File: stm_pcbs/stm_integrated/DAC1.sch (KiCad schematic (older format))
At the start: 21 parts, among them P2 BNC, U4 AD8676, U5 AD5791, U6 AD8675

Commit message: working on Kicad of 3rd Dec
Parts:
- C17, C19, C21, C23, C24, C27, C28, C31, C32: symbol C -> device:C
- C18, C20, C22, C25, C26, C29, C30: symbol CP2 -> device:CP1
- P2: symbol BNC -> device:BNC
- R2: symbol R -> device:R
- U4: symbol AD8676 -> ad5791:AD8676
- U5: symbol AD5791 -> ad5791:AD5791
- U6: symbol AD8675 -> ad5791:AD8675
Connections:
- wire segments 113 -> 128

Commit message: fixing more borkage
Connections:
- net labels added: +5V
- net labels removed: 3.3V
- wire segments 128 -> 123
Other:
- moved on the sheet: C21, C22, R2
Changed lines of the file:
@@
 Text GLabel 5350 4950 2    60   Input ~ 0
 -14V
-Text GLabel 4250 2400 0    60   Input ~ 0
-3.3V
 $Comp
 L power:AGND #PWR014
@@
 L device:C C21
 U 1 1 5A25DC09
-P 6000 4700
+P 6000 4650
 AR Path="/5A25DC09" Ref="C21"  Part="1"
 AR Path="/5A25907D/5A25DC09" Ref="C21"  Part="1"
-F 0 "C21" H 6000 4800 40  0000 L CNN
-F 1 "0.1uF" H 6006 4615 40  0000 L CNN
-F 2 "Capacitors_SMD:C_0805_HandSoldering" H 6038 4550 30  0001 C CNN
-F 3 "" H 6000 4700 60  0000 C CNN
-	1    6000 4700
+F 0 "C21" H 6000 4750 40  0000 L CNN
+F 1 "0.1uF" H 6006 4565 40  0000 L CNN
+F 2 "Capacitors_SMD:C_0805_HandSoldering" H 6038 4500 30  0001 C CNN
+F 3 "" H 6000 4650 60  0000 C CNN
+	1    6000 4650
 	0    1    1    0
 $EndComp
@@
 L device:CP1 C22
 U 1 1 5A25DC67
-P 6000 4950
+P 6000 5000
 AR Path="/5A25DC67" Ref="C22"  Part="1"
 AR Path="/5A25907D/5A25DC67" Ref="C22"  Part="1"
-F 0 "C22" H 6000 5050 40  0000 L CNN
-F 1 "10uF" H 6006 4865 40  0000 L CNN
-F 2 "stm:SMD-1210_Pol" H 6038 4800 30  0001 C CNN
-F 3 "" H 6000 4950 60  0000 C CNN
-	1    6000 4950
+F 0 "C22" H 6000 5100 40  0000 L CNN
+F 1 "10uF" H 6006 4915 40  0000 L CNN
+F 2 "stm:SMD-1210_Pol" H 6038 4850 30  0001 C CNN
+F 3 "" H 6000 5000 60  0000 C CNN
+	1    6000 5000
 	0    1    1    0
 $EndComp
@@
 	7850 3750 7850 3900
 Wire Wire Line
-	5600 2050 5600 2300
-Wire Wire Line
 	5300 4800 5300 4950
 Wire Wire Line
@@
 Connection ~ 4650 2500
 Wire Wire Line
-	4400 2400 4250 2400
-Wire Wire Line
 	4850 5000 4850 4800
 Wire Wire Line
@@
 Wire Wire Line
 	5250 2450 5250 2700
-Wire Wire Line
-	5600 2300 5700 2300
-Connection ~ 5600 2300
 Wire Wire Line
 	5650 2550 5650 2400
@@
 Wire Wire Line
 	5300 4800 5800 4800
-Wire Wire Line
-	5800 4700 5800 4800
-Wire Wire Line
-	6200 4700 6200 4800
 Connection ~ 5800 4800
 Wire Wire Line
@@
 L device:R R2
 U 1 1 5A25DD1F
-P 7150 4650
+P 7150 4550
 AR Path="/5A25DD1F" Ref="R2"  Part="1"
 AR Path="/5A25907D/5A25DD1F" Ref="R2"  Part="1"
-F 0 "R2" V 7230 4650 40  0000 C CNN
-F 1 "0" V 7157 4651 40  0000 C CNN
-F 2 "stm:0Ohm" V 7080 4650 30  0001 C CNN
-F 3 "" H 7150 4650 30  0000 C CNN
-	1    7150 4650
+F 0 "R2" V 7230 4550 40  0000 C CNN
+F 1 "0" V 7157 4551 40  0000 C CNN
+F 2 "stm:0Ohm" V 7080 4550 30  0001 C CNN
+F 3 "" H 7150 4550 30  0000 C CNN
+	1    7150 4550
 	0    1    1    0
 $EndComp
@@
 $EndComp
 Wire Wire Line
-	7400 4750 7400 4650
-Wire Wire Line
-	6900 4650 6900 4750
-Wire Wire Line
-	7600 3750 7600 3800
-Wire Wire Line
-	7600 4150 7600 4100
-Wire Wire Line
-	7400 4650 7300 4650
-Wire Wire Line
-	7000 4650 6900 4650
-Wire Wire Line
-	6150 4700 6200 4700
-Wire Wire Line
-	5850 4700 5800 4700
-Wire Wire Line
-	7600 3000 7600 3050
-Wire Wire Line
-	7600 3400 7600 3350
-Wire Wire Line
 	3850 2150 3850 2200
 Wire Wire Line
 	3850 1850 3850 1800
-Wire Wire Line
-	6000 2300 6050 2300
 Wire Wire Line
 	3200 3300 3850 3300
@@
 	4650 2500 4800 2500
 Wire Wire Line
+	5600 2400 5600 2450
+Wire Wire Line
+	6050 2400 6050 2550
+Wire Wire Line
+	4450 2500 4650 2500
+Wire Wire Line
+	3950 1800 4100 1800
+Wire Wire Line
+	7600 5350 7700 5350
+Wire Wire Line
+	7250 5500 7350 5500
+Wire Wire Line
+	7250 5900 7350 5900
+Wire Wire Line
+	8600 5350 8750 5350
+Wire Wire Line
+	7700 5350 7800 5350
+Wire Wire Line
+	6850 3200 6950 3200
+Wire Wire Line
+	6850 3900 6900 3900
+Wire Wire Line
+	8750 6300 8750 6350
+Wire Wire Line
+	8750 5750 8750 5800
+Wire Wire Line
+	3850 2200 4100 2200
+Wire Wire Line
+	7250 6050 7700 6050
+Wire Wire Line
+	7700 6050 7800 6050
+Wire Wire Line
+	6850 3000 7400 3000
+Wire Wire Line
+	6850 3750 7400 3750
+Wire Wire Line
+	7750 5900 8750 5900
+Wire Wire Line
+	7300 3400 7400 3400
+Wire Wire Line
+	7400 4550 7400 4750
+Wire Wire Line
+	6900 4550 6900 4750
+Wire Wire Line
+	6200 4800 6200 5000
+Wire Wire Line
+	5800 4800 5800 5000
+Wire Wire Line
+	6200 4650 6200 4800
+Wire Wire Line
+	5800 4650 5800 4800
+Connection ~ 7400 3000
+Wire Wire Line
+	7400 3000 7600 3000
+Connection ~ 7400 3400
+Wire Wire Line
+	7400 3400 7600 3400
+Connection ~ 7400 3750
+Wire Wire Line
+	7400 3750 7600 3750
+Connection ~ 7400 4150
+Wire Wire Line
+	5600 2050 5600 2300
+Wire Wire Line
+	5650 2300 5600 2300
+Connection ~ 5600 2300
+Wire Wire Line
 	5600 2300 5600 2400
-Wire Wire Line
-	5600 2400 5600 2450
-Wire Wire Line
-	6050 2400 6050 2550
-Wire Wire Line
-	5800 4800 5800 4950
-Wire Wire Line
-	6200 4800 6200 4950
-Wire Wire Line
-	4450 2500 4650 2500
-Wire Wire Line
-	3950 1800 4100 1800
-Wire Wire Line
-	7600 5350 7700 5350
-Wire Wire Line
-	7250 5500 7350 5500
-Wire Wire Line
-	7250 5900 7350 5900
-Wire Wire Line
-	8600 5350 8750 5350
-Wire Wire Line
-	7700 5350 7800 5350
-Wire Wire Line
-	6850 3200 6950 3200
-Wire Wire Line
-	6850 3900 6900 3900
-Wire Wire Line
-	8750 6300 8750 6350
-Wire Wire Line
-	8750 5750 8750 5800
-Wire Wire Line
-	3850 2200 4450 2200
-Wire Wire Line
-	7250 6050 7700 6050
-Wire Wire Line
-	7700 6050 7800 6050
-Wire Wire Line
-	6850 3000 7600 3000
-Wire Wire Line
-	6850 3750 7600 3750
-Wire Wire Line
-	7750 5900 8750 5900
-Wire Wire Line
-	7300 3400 7600 3400
+Connection ~ 4100 2200
+Wire Wire Line
+	4100 2200 4450 2200
+Connection ~ 3850 1800
+Connection ~ 3850 2200
+Connection ~ 7350 5500
+Connection ~ 7350 5900
+$Comp
+L power:+5V #PWR?
+U 1 1 5A4D419F
+P 4200 2400
+F 0 "#PWR?" H 4200 2490 20  0001 C CNN
+F 1 "+5V" H 4196 2528 30  0000 C CNN
+F 2 "" H 4200 2400 60  0001 C CNN
+F 3 "" H 4200 2400 60  0001 C CNN
+	1    4200 2400
+	1    0    0    -1
+$EndComp
+Wire Wire Line
+	4200 2400 4400 2400
 $EndSCHEMATC

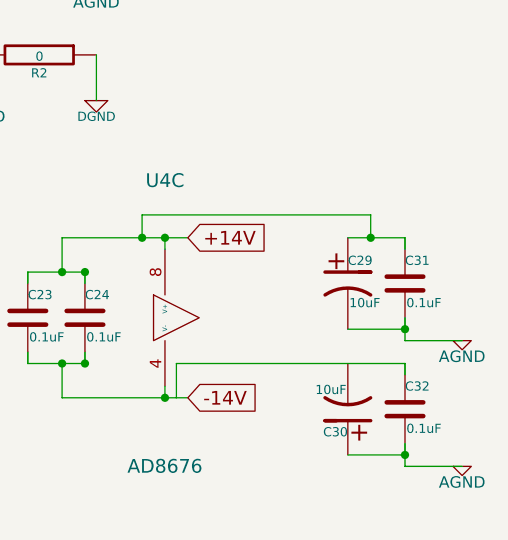
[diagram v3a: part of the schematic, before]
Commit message: Using LTZ1000 (A9 board)
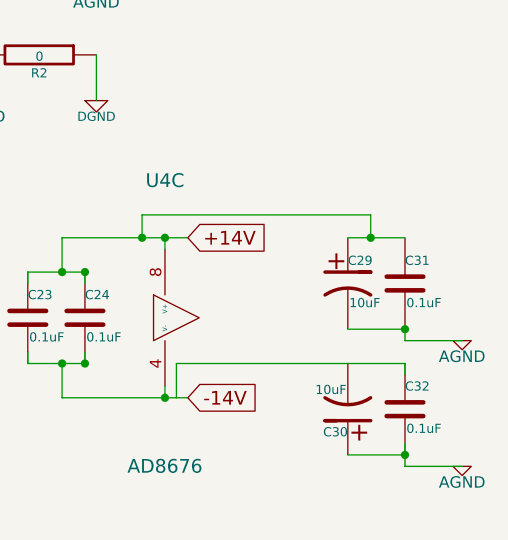
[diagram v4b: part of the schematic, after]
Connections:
- wire segments 123 -> 121
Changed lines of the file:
@@
 	8750 5800 9000 5800
-Wire Wire Line
-	8750 5700 8750 5750
 Wire Wire Line
 	8750 6350 9000 6350
@@
 Connection ~ 8750 5750
 Wire Wire Line
-	8750 5350 8750 5400
-Wire Wire Line
 	7150 3550 7700 3550
